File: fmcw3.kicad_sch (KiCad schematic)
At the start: 13 parts, among them P5 CONN_01X01, P7 CONN_01X01, P8 CONN_01X01, U6 PL133-37, Y2 ECS-TXO-32CSMV

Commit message: final changes
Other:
- title: (none) -> FMCW3 by CENK KESKİN
- moved on the sheet: C1, C12, C17, FB1, P5, P7, P8, R13, R15, R16, R19, U6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

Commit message: hardware changes
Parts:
- removed C1, C17: 100n, Footprints:SMD_0402, symbol fmcw3-rescue:C
- removed C12: 1u, Footprints:SMD_0603, symbol fmcw3-rescue:C
- removed FB1: BLM18PG181SN1D, Footprints:SMD_0603, symbol fmcw3-rescue:FILTER
- removed P5, P7, P8: CONN_01X01, fmcw3:MountingHole_3.2mm_M3_Pad_Via_mod, symbol fmcw3-rescue:CONN_01X01
- removed R13, R15, R16: 33, Footprints:SMD_0402, symbol fmcw3-rescue:R
- removed R19: 0, Footprints:SMD_0402, symbol Resistor:Resistor
- removed U6: PL133-37, Footprints:SOT23_6, symbol PL133_37:PL133_37
- removed Y2: ECS-TXO-32CSMV, Oscillator:Oscillator_SMD_ECS_2520MV-xxx-xx-4Pin_2.5x2.0mm, symbol ECS-TXO-32CSMV:ECS-TXO-32CSMV
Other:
- added sheet clock (clock.kicad_sch)
- sheet fpga ports: added FPGA_CLK; removed CLK_REF
- sheet tx ports: added ADF_CLK_REF; removed REFIN
- note removed: "10V: 5 mA 3.3V current: 35mA 3.0V current: 27mA 5V current: 750mA"
- note removed: "1V0: 100 mA 1V8: 30 mA 3V0: 170 mA 5V: 900 mA 3.3VA: 540 mA 3.3VD: 100 mA 3V8: 80 mA 10V: 5 mA"
- note removed: "1V0: 100 mA 1V8: 30 mA 3V6: 80 mA 3V3D: 70 mA"
- note removed: "20 mA"
- note removed: "3V0: 70 mA"
- note removed: "5V: 200 mA"
- note removed: "DC removing cap might be needed. Place 10nF cap or 0 ohm resistor. TXO is clipped sine this time."
- note removed: "Power: TX: 1.65 W LNA: 0.45 W Digital: 0.7 W Mixer: 1.0 W IF: 0.01 W Clock: 0.1 W = 4 W"
- note removed: "This is the prev design: NB3N551 is obs. Also this txo is generating pure sin. ADC might need cmos like input not sin. That could be the reason of duty stabilizer."

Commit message: schematic is updated pcb is almost done
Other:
- sheet if renamed opamp_amp
- sheet fpga ports: added ADC_VCMA, ADC_VCMB; removed ADC_VCM1, ADC_VCM2
- sheet opamp_amp: file if.kicad_sch -> opamp_amp.kicad_sch
- sheet opamp_amp ports: added VCMA, VCMB; removed VCOM1, VCOM2
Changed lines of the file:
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@@
 		)
 	)
-	(label "ADC_VCM2"
+	(label "ADC_VCMB"
 		(at 83.82 50.8 180)
 		(effects
@@
 		)
 	)
-	(label "ADC_VCM1"
+	(label "ADC_VCMA"
 		(at 193.04 109.22 0)
 		(effects
@@
 		)
 	)
-	(label "ADC_VCM1"
+	(label "ADC_VCMA"
 		(at 83.82 41.91 180)
 		(effects
@@
 		)
 	)
-	(label "ADC_VCM2"
+	(label "ADC_VCMB"
 		(at 193.04 111.76 0)
 		(effects
@@
 			)
 		)
-		(pin "ADC_VCM1" output
+		(pin "ADC_VCMA" output
 			(at 88.9 41.91 180)
 			(effects
@@
 			)
 		)
-		(pin "ADC_VCM2" output
+		(pin "ADC_VCMB" output
 			(at 88.9 50.8 180)
 			(effects
@@
 			(color 0 0 0 0.0000)
 		)
-		(property "Sheetname" "if"
+		(property "Sheetname" "opamp_amp"
 			(at 162.56 93.1414 0)
 			(effects
@@
 			)
 		)
-		(property "Sheetfile" "if.kicad_sch"
+		(property "Sheetfile" "opamp_amp.kicad_sch"
 			(at 162.56 120.0662 0)
 			(effects
@@
 			)
 		)
-		(pin "VCOM1" input
+		(pin "VCMA" input
 			(at 190.5 109.22 0)
 			(effects
@@
 			)
 		)
-		(pin "VCOM2" input
+		(pin "VCMB" input
 			(at 190.5 111.76 0)
 			(effects

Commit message: lt6232 is done. I push latest updates
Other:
- note removed: "3V3A: 5 mA"
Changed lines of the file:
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@@
 		(title "FMCW3 by CENK KESKİN")
-	)
-	(text "3V3A: 5 mA"
-		(exclude_from_sim no)
-		(at 193.04 120.65 0)
-		(effects
-			(font
-				(size 1.524 1.524)
-			)
-			(justify left bottom)
-		)
 	)
 	(wire

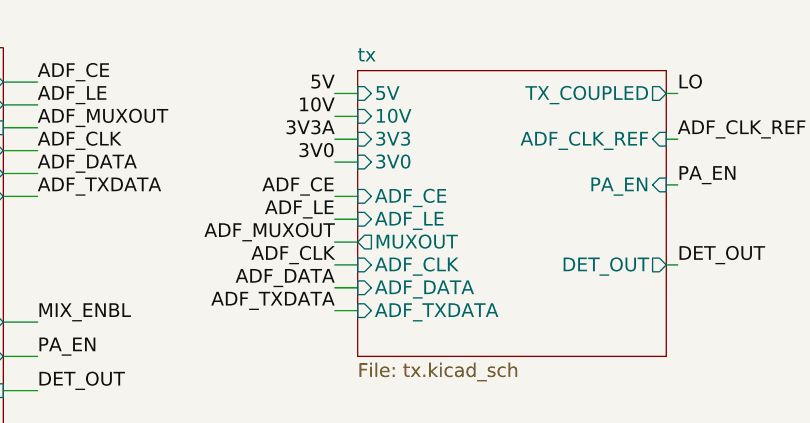
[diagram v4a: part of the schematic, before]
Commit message: pcb is checked dnp is deleted copper pours are checked
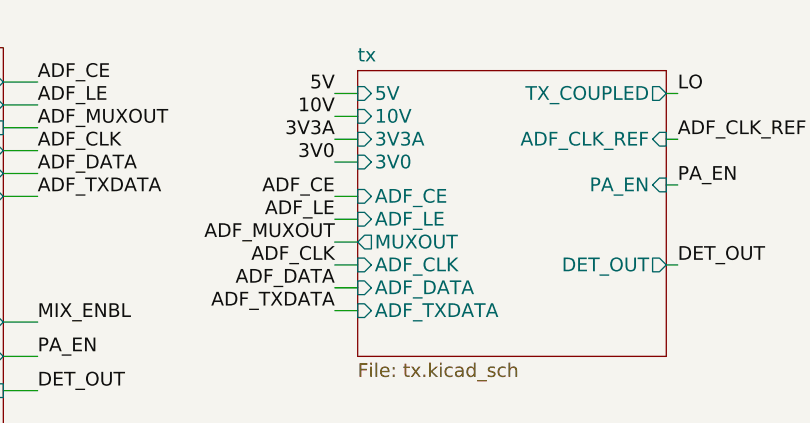
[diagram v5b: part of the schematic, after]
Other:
- sheet tx ports: added 3V3A; removed 3V3
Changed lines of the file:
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@@
 			)
 		)
-		(pin "3V3" input
+		(pin "3V3A" input
 			(at 168.91 43.18 180)
 			(effects
